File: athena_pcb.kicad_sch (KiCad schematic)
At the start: 32 parts, among them J1 Conn_02x03_Odd_Even, SW1 SW_Push, SW2 SW_Push, U1 NRF5340-QKAA-R7, U2 BME280, Y1 32MHz, Y2 32.768kHz

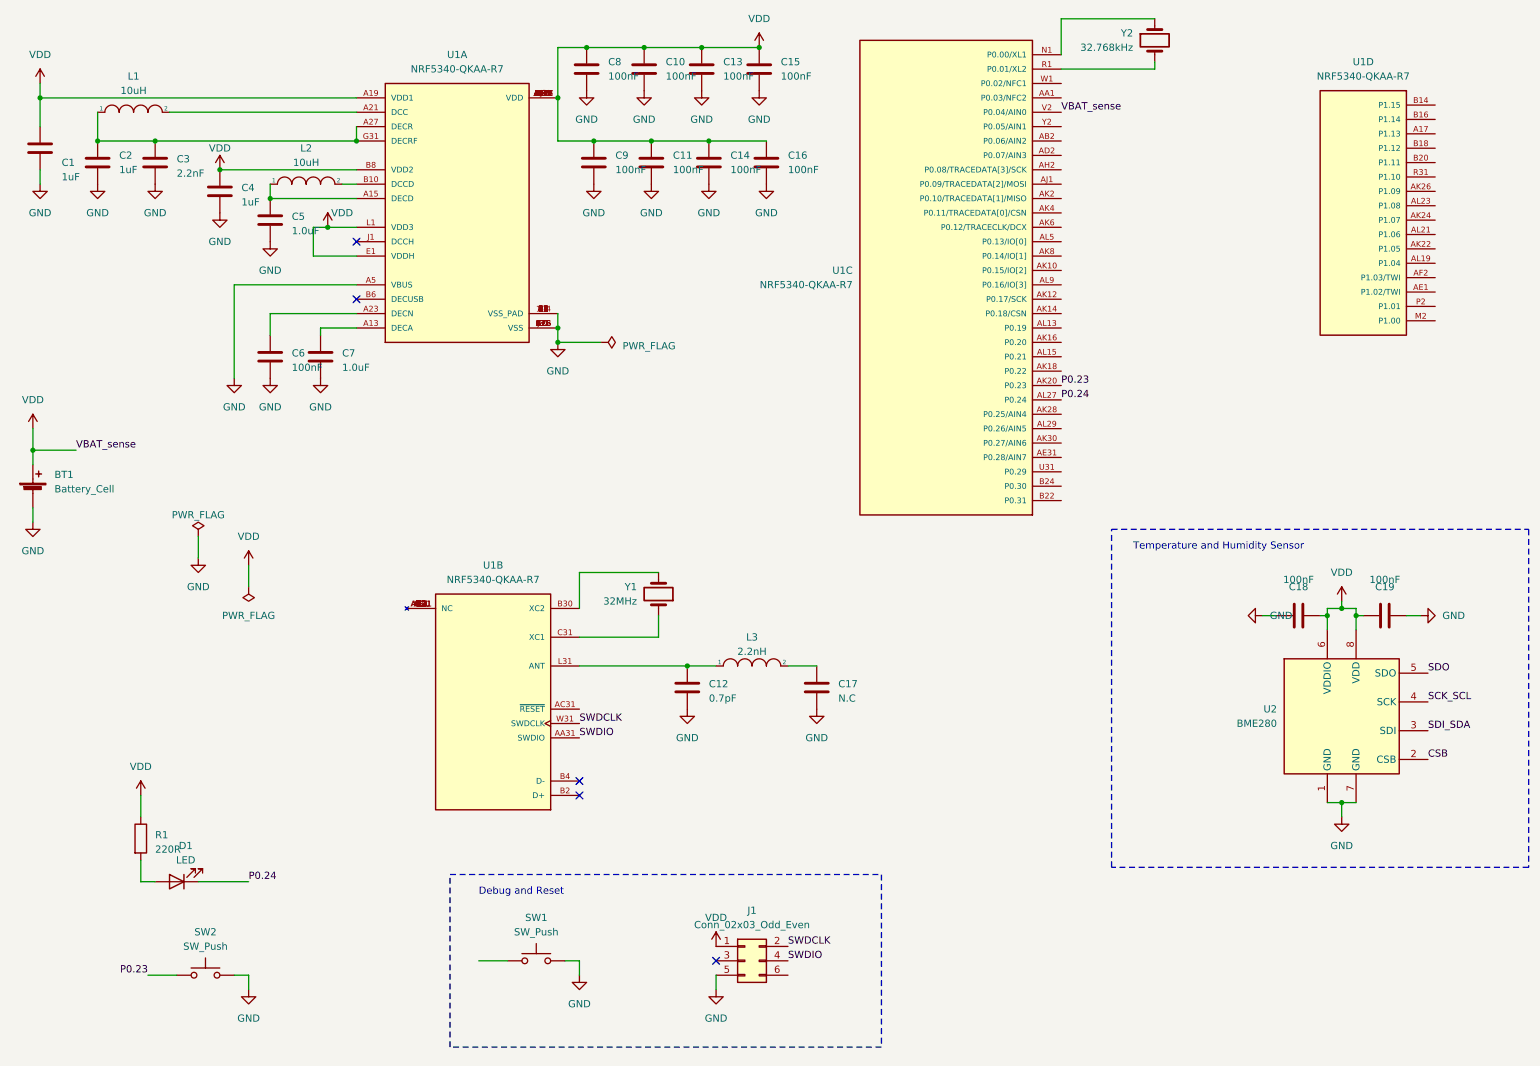
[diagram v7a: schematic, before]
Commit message: Added board layout constraints
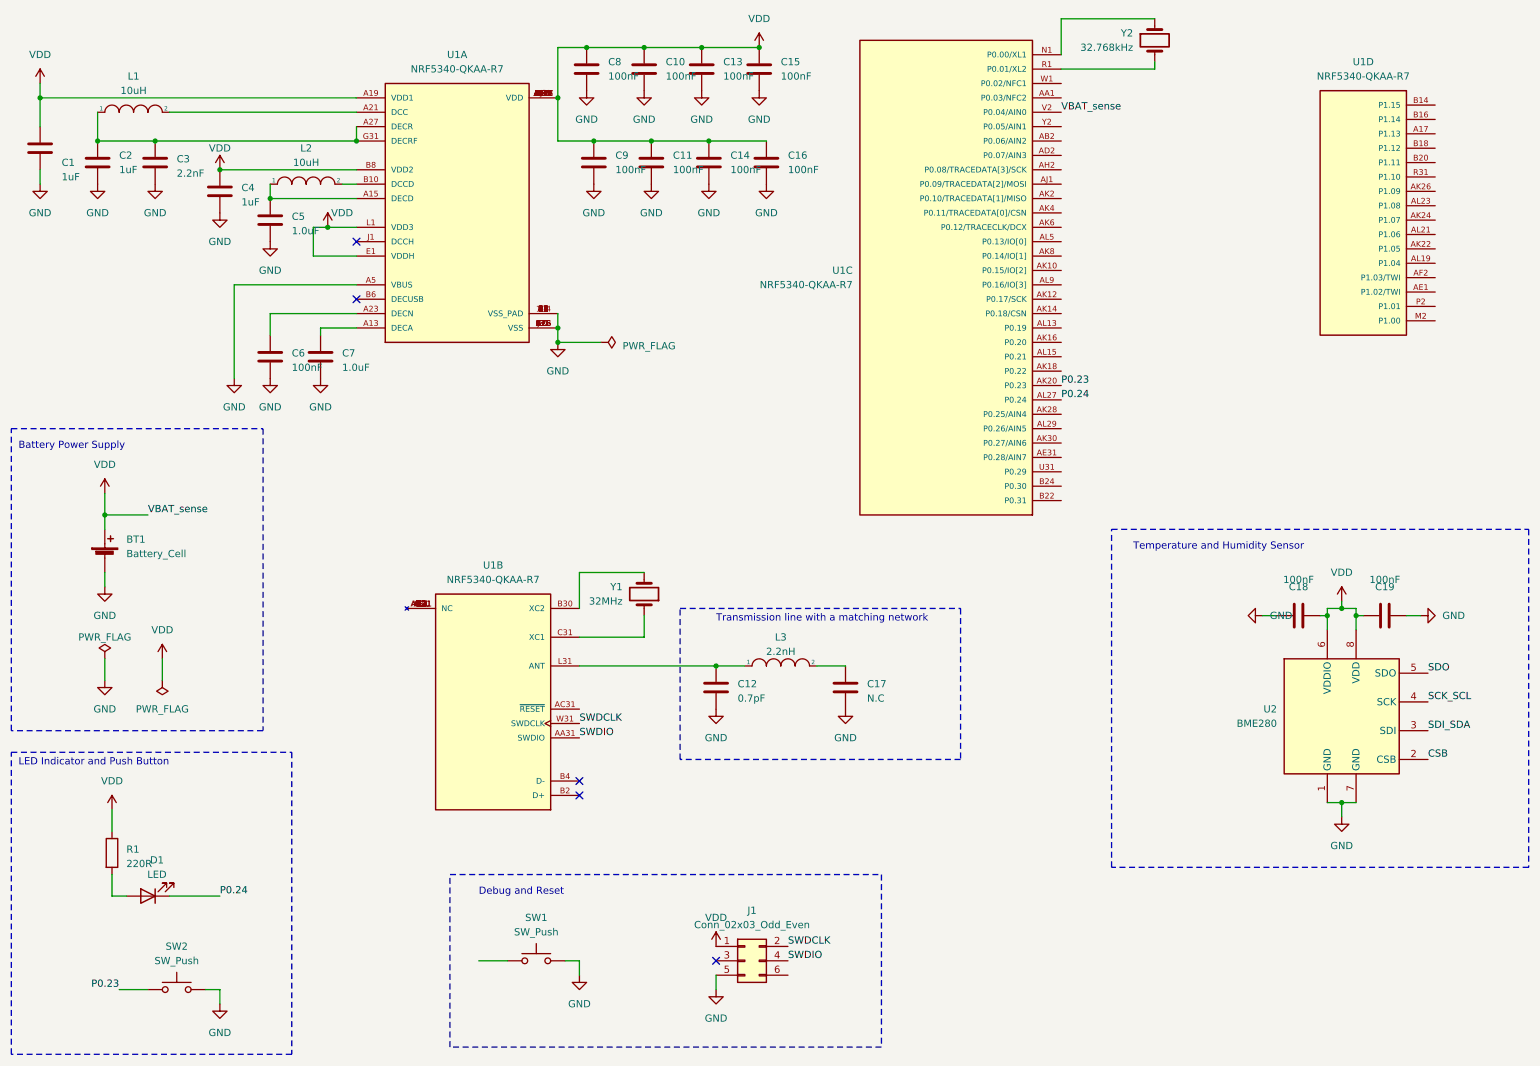
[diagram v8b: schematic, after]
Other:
- note added: "Battery Power Supply"
- note added: "LED Indicator and Push Button"
- note added: "Transmission line with a matching network"
- title: (none) -> Project Athena
- moved on the sheet: BT1, C12, C17, D1, L3, R1, SW2, Y1
